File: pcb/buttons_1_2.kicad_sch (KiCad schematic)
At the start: 39 parts, among them J12 Conn_01x07_Male, SW10 Reset, SW11 +1, SW12 +10, SW13 -10, SW14 -1, SW15 x2, SW16 /2, SW17 Random, SW2 Reset, SW3 +1, SW4 +10, SW5 -10, SW6 -1, SW7 x2, SW8 /2, SW9 Random, U7 74HC165, U8 74HC165

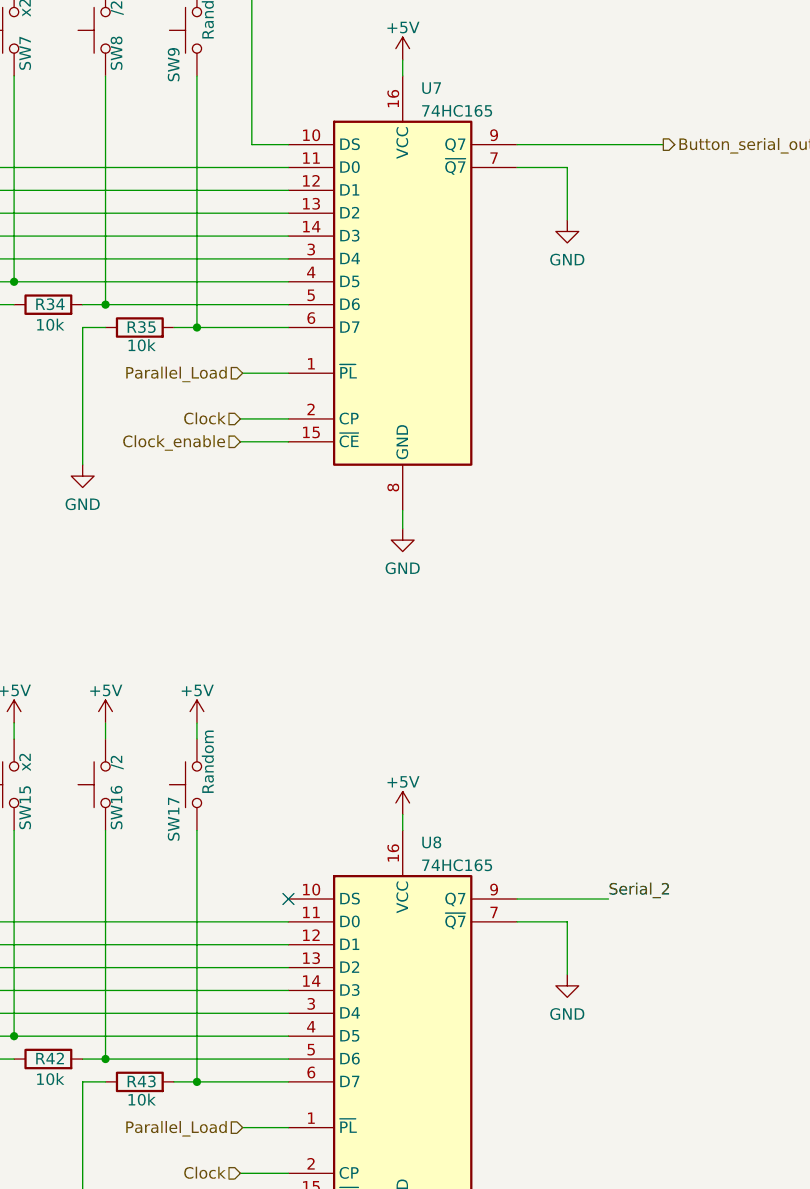
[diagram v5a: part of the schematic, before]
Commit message: moved crystal
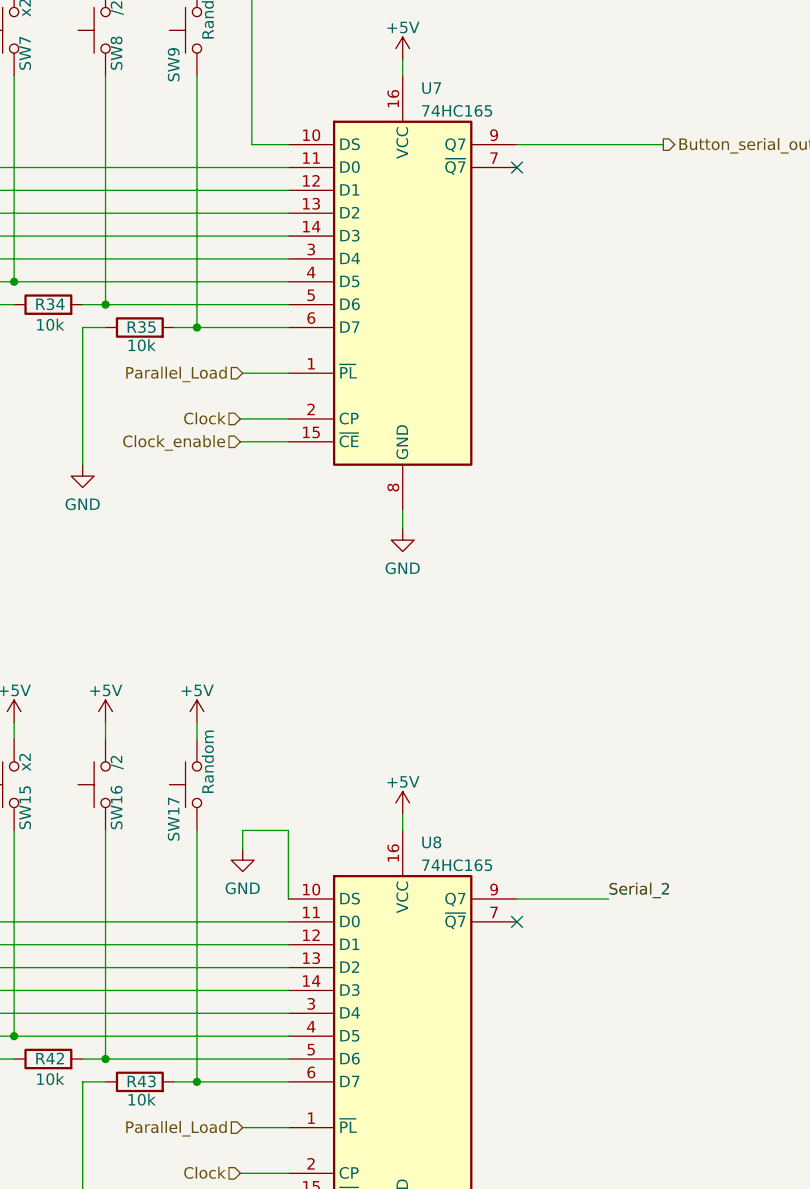
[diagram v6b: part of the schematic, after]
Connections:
- net GND: now also U8.10 (DS); no longer U7.7 (~{Q7}), U8.7 (~{Q7})
- no-connect marks 1 -> 2
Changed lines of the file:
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@@
   (junction (at 99.06 60.96) (diameter 0) (color 0 0 0 0)
   )
-  (no_connect (at 139.7 132.08))
+  (no_connect (at 165.1 134.62))
+  (no_connect (at 165.1 50.8))
   (wire (pts (xy 218.44 124.46) (xy 238.76 124.46))
     (stroke (width 0) (type default) (color 0 0 0 0))
@@
     (stroke (width 0) (type default) (color 0 0 0 0))
   )
+  (wire (pts (xy 134.62 124.46) (xy 134.62 126.492))
+    (stroke (width 0) (type default) (color 0 0 0 0))
+  )
   (wire (pts (xy 66.04 142.24) (xy 66.04 167.64))
     (stroke (width 0) (type default) (color 0 0 0 0))
@@
     (stroke (width 0) (type default) (color 0 0 0 0))
   )
+  (wire (pts (xy 139.7 124.46) (xy 139.7 132.08))
+    (stroke (width 0) (type default) (color 0 0 0 0))
+  )
   (wire (pts (xy 78.74 144.78) (xy 78.74 167.64))
     (stroke (width 0) (type default) (color 0 0 0 0))
@@
     (stroke (width 0) (type default) (color 0 0 0 0))
   )
+  (wire (pts (xy 134.62 124.46) (xy 139.7 124.46))
+    (stroke (width 0) (type default) (color 0 0 0 0))
+  )
   (wire (pts (xy 96.52 63.5) (xy 91.44 63.5))
     (stroke (width 0) (type default) (color 0 0 0 0))
@@
     (stroke (width 0) (type default) (color 0 0 0 0))
   )
-  (wire (pts (xy 165.1 50.8) (xy 170.688 50.8))
-    (stroke (width 0) (type default) (color 0 0 0 0))
-  )
   (wire (pts (xy 58.42 139.7) (xy 53.34 139.7))
     (stroke (width 0) (type default) (color 0 0 0 0))
@@
     (stroke (width 0) (type default) (color 0 0 0 0))
   )
-  (wire (pts (xy 170.688 50.8) (xy 170.688 56.642))
-    (stroke (width 0) (type default) (color 0 0 0 0))
-  )
   (wire (pts (xy 91.44 60.96) (xy 99.06 60.96))
     (stroke (width 0) (type default) (color 0 0 0 0))
@@
     (stroke (width 0) (type default) (color 0 0 0 0))
   )
-  (wire (pts (xy 165.1 134.62) (xy 170.688 134.62))
-    (stroke (width 0) (type default) (color 0 0 0 0))
-  )
   (wire (pts (xy 91.44 63.5) (xy 91.44 83.82))
     (stroke (width 0) (type default) (color 0 0 0 0))
@@
   )
   (wire (pts (xy 165.1 132.08) (xy 175.26 132.08))
-    (stroke (width 0) (type default) (color 0 0 0 0))
-  )
-  (wire (pts (xy 170.688 134.62) (xy 170.688 140.462))
     (stroke (width 0) (type default) (color 0 0 0 0))
   )
@@
     )
     (property "Datasheet" "" (id 3) (at 27.94 83.82 0)
-      (effects (font (size 1.27 1.27)) hide)
-    )
-    (pin "1")
-  )
-  (symbol (lib_id "power:GND") (at 170.688 140.462 0) (unit 1)
-    (in_bom yes) (on_board yes) (fields_autoplaced)
-    (property "Reference" "#PWR037" (id 0) (at 170.688 146.812 0)
-      (effects (font (size 1.27 1.27)) hide)
-    )
-    (property "Value" "GND" (id 1) (at 170.688 144.9054 0))
-    (property "Footprint" "" (id 2) (at 170.688 140.462 0)
-      (effects (font (size 1.27 1.27)) hide)
-    )
-    (property "Datasheet" "" (id 3) (at 170.688 140.462 0)
       (effects (font (size 1.27 1.27)) hide)
     )
@@
     (pin "1")
   )
+  (symbol (lib_id "power:GND") (at 134.62 126.492 0) (unit 1)
+    (in_bom yes) (on_board yes) (fields_autoplaced)
+    (property "Reference" "#PWR0166" (id 0) (at 134.62 132.842 0)
+      (effects (font (size 1.27 1.27)) hide)
+    )
+    (property "Value" "GND" (id 1) (at 134.62 130.9354 0))
+    (property "Footprint" "" (id 2) (at 134.62 126.492 0)
+      (effects (font (size 1.27 1.27)) hide)
+    )
+    (property "Datasheet" "" (id 3) (at 134.62 126.492 0)
+      (effects (font (size 1.27 1.27)) hide)
+    )
+    (pin "1")
+  )
   (symbol (lib_id "Switch:SW_Push") (at 109.22 119.38 90) (unit 1)
     (in_bom yes) (on_board yes)
@@
     (pin "2")
   )
-  (symbol (lib_id "power:GND") (at 170.688 56.642 0) (unit 1)
-    (in_bom yes) (on_board yes) (fields_autoplaced)
-    (property "Reference" "#PWR018" (id 0) (at 170.688 62.992 0)
-      (effects (font (size 1.27 1.27)) hide)
-    )
-    (property "Value" "GND" (id 1) (at 170.688 61.0854 0))
-    (property "Footprint" "" (id 2) (at 170.688 56.642 0)
-      (effects (font (size 1.27 1.27)) hide)
-    )
-    (property "Datasheet" "" (id 3) (at 170.688 56.642 0)
-      (effects (font (size 1.27 1.27)) hide)
-    )
-    (pin "1")
-  )
   (symbol (lib_id "Switch:SW_Push") (at 58.42 35.56 90) (unit 1)

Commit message: new layout with usb
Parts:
- R28, R29, R30, R31, R32, R33, R34, R35, R36, R37, R38, R39, R40, R41, R42, R43: footprint Resistor_THT:R_Axial_DIN0207_L6.3mm_D2.5mm_P7.62mm_Horizontal -> Resistor_THT:R_Axial_DIN0207_L6.3mm_D2.5mm_P10.16mm_Horizontal
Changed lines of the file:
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@@
       (effects (font (size 1.27 1.27)) (justify left))
     )
-    (property "Footprint" "Resistor_THT:R_Axial_DIN0207_L6.3mm_D2.5mm_P7.62mm_Horizontal" (id 2) (at 100.33 65.278 90)
+    (property "Footprint" "Resistor_THT:R_Axial_DIN0207_L6.3mm_D2.5mm_P10.16mm_Horizontal" (id 2) (at 100.33 65.278 90)
       (effects (font (size 1.27 1.27)) hide)
     )
@@
       (effects (font (size 1.27 1.27)) (justify left))
     )
-    (property "Footprint" "Resistor_THT:R_Axial_DIN0207_L6.3mm_D2.5mm_P7.62mm_Horizontal" (id 2) (at 49.53 138.938 90)
+    (property "Footprint" "Resistor_THT:R_Axial_DIN0207_L6.3mm_D2.5mm_P10.16mm_Horizontal" (id 2) (at 49.53 138.938 90)
       (effects (font (size 1.27 1.27)) hide)
     )
@@
       (effects (font (size 1.27 1.27)) (justify left))
     )
-    (property "Footprint" "Resistor_THT:R_Axial_DIN0207_L6.3mm_D2.5mm_P7.62mm_Horizontal" (id 2) (at 36.83 136.398 90)
+    (property "Footprint" "Resistor_THT:R_Axial_DIN0207_L6.3mm_D2.5mm_P10.16mm_Horizontal" (id 2) (at 36.83 136.398 90)
       (effects (font (size 1.27 1.27)) hide)
     )
@@
       (effects (font (size 1.27 1.27)) (justify left))
     )
-    (property "Footprint" "Resistor_THT:R_Axial_DIN0207_L6.3mm_D2.5mm_P7.62mm_Horizontal" (id 2) (at 113.03 151.638 90)
+    (property "Footprint" "Resistor_THT:R_Axial_DIN0207_L6.3mm_D2.5mm_P10.16mm_Horizontal" (id 2) (at 113.03 151.638 90)
       (effects (font (size 1.27 1.27)) hide)
     )
@@
       (effects (font (size 1.27 1.27)) (justify left))
     )
-    (property "Footprint" "Resistor_THT:R_Axial_DIN0207_L6.3mm_D2.5mm_P7.62mm_Horizontal" (id 2) (at 113.03 67.818 90)
+    (property "Footprint" "Resistor_THT:R_Axial_DIN0207_L6.3mm_D2.5mm_P10.16mm_Horizontal" (id 2) (at 113.03 67.818 90)
       (effects (font (size 1.27 1.27)) hide)
     )
@@
       (effects (font (size 1.27 1.27)) (justify left))
     )
-    (property "Footprint" "Resistor_THT:R_Axial_DIN0207_L6.3mm_D2.5mm_P7.62mm_Horizontal" (id 2) (at 123.19 154.178 90)
+    (property "Footprint" "Resistor_THT:R_Axial_DIN0207_L6.3mm_D2.5mm_P10.16mm_Horizontal" (id 2) (at 123.19 154.178 90)
       (effects (font (size 1.27 1.27)) hide)
     )
@@
       (effects (font (size 1.27 1.27)) (justify left))
     )
-    (property "Footprint" "Resistor_THT:R_Axial_DIN0207_L6.3mm_D2.5mm_P7.62mm_Horizontal" (id 2) (at 49.53 55.118 90)
+    (property "Footprint" "Resistor_THT:R_Axial_DIN0207_L6.3mm_D2.5mm_P10.16mm_Horizontal" (id 2) (at 49.53 55.118 90)
       (effects (font (size 1.27 1.27)) hide)
     )
@@
       (effects (font (size 1.27 1.27)) (justify left))
     )
-    (property "Footprint" "Resistor_THT:R_Axial_DIN0207_L6.3mm_D2.5mm_P7.62mm_Horizontal" (id 2) (at 100.33 149.098 90)
+    (property "Footprint" "Resistor_THT:R_Axial_DIN0207_L6.3mm_D2.5mm_P10.16mm_Horizontal" (id 2) (at 100.33 149.098 90)
       (effects (font (size 1.27 1.27)) hide)
     )
@@
       (effects (font (size 1.27 1.27)) (justify left))
     )
-    (property "Footprint" "Resistor_THT:R_Axial_DIN0207_L6.3mm_D2.5mm_P7.62mm_Horizontal" (id 2) (at 62.23 57.658 90)
+    (property "Footprint" "Resistor_THT:R_Axial_DIN0207_L6.3mm_D2.5mm_P10.16mm_Horizontal" (id 2) (at 62.23 57.658 90)
       (effects (font (size 1.27 1.27)) hide)
     )
@@
       (effects (font (size 1.27 1.27)) (justify left))
     )
-    (property "Footprint" "Resistor_THT:R_Axial_DIN0207_L6.3mm_D2.5mm_P7.62mm_Horizontal" (id 2) (at 62.23 141.478 90)
+    (property "Footprint" "Resistor_THT:R_Axial_DIN0207_L6.3mm_D2.5mm_P10.16mm_Horizontal" (id 2) (at 62.23 141.478 90)
       (effects (font (size 1.27 1.27)) hide)
     )
@@
       (effects (font (size 1.27 1.27)) (justify left))
     )
-    (property "Footprint" "Resistor_THT:R_Axial_DIN0207_L6.3mm_D2.5mm_P7.62mm_Horizontal" (id 2) (at 87.63 146.558 90)
+    (property "Footprint" "Resistor_THT:R_Axial_DIN0207_L6.3mm_D2.5mm_P10.16mm_Horizontal" (id 2) (at 87.63 146.558 90)
       (effects (font (size 1.27 1.27)) hide)
     )
@@
       (effects (font (size 1.27 1.27)) (justify left))
     )
-    (property "Footprint" "Resistor_THT:R_Axial_DIN0207_L6.3mm_D2.5mm_P7.62mm_Horizontal" (id 2) (at 75.184 144.018 90)
+    (property "Footprint" "Resistor_THT:R_Axial_DIN0207_L6.3mm_D2.5mm_P10.16mm_Horizontal" (id 2) (at 75.184 144.018 90)
       (effects (font (size 1.27 1.27)) hide)
     )
@@
       (effects (font (size 1.27 1.27)) (justify left))
     )
-    (property "Footprint" "Resistor_THT:R_Axial_DIN0207_L6.3mm_D2.5mm_P7.62mm_Horizontal" (id 2) (at 75.184 60.198 90)
+    (property "Footprint" "Resistor_THT:R_Axial_DIN0207_L6.3mm_D2.5mm_P10.16mm_Horizontal" (id 2) (at 75.184 60.198 90)
       (effects (font (size 1.27 1.27)) hide)
     )
@@
       (effects (font (size 1.27 1.27)) (justify left))
     )
-    (property "Footprint" "Resistor_THT:R_Axial_DIN0207_L6.3mm_D2.5mm_P7.62mm_Horizontal" (id 2) (at 123.19 70.358 90)
+    (property "Footprint" "Resistor_THT:R_Axial_DIN0207_L6.3mm_D2.5mm_P10.16mm_Horizontal" (id 2) (at 123.19 70.358 90)
       (effects (font (size 1.27 1.27)) hide)
     )
@@
       (effects (font (size 1.27 1.27)) (justify left))
     )
-    (property "Footprint" "Resistor_THT:R_Axial_DIN0207_L6.3mm_D2.5mm_P7.62mm_Horizontal" (id 2) (at 87.63 62.738 90)
+    (property "Footprint" "Resistor_THT:R_Axial_DIN0207_L6.3mm_D2.5mm_P10.16mm_Horizontal" (id 2) (at 87.63 62.738 90)
       (effects (font (size 1.27 1.27)) hide)
     )
@@
       (effects (font (size 1.27 1.27)) (justify left))
     )
-    (property "Footprint" "Resistor_THT:R_Axial_DIN0207_L6.3mm_D2.5mm_P7.62mm_Horizontal" (id 2) (at 36.83 52.578 90)
-      (effects (font (size 1.27 1.27)) hide)
-    )
+    (property "Footprint" "Resistor_THT:R_Axial_DIN0207_L6.3mm_D2.5mm_P10.16mm_Horizontal" (id 2) (at 36.83 52.578 90)
+      (effects (font (size 1.27 1.27)) hide)
+    )
